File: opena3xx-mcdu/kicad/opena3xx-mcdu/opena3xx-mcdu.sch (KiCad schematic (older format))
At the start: 48 parts, among them J1 Conn_02x01, J2 Conn_02x01, J3 Conn_02x01, J4 Conn_02x01, J5 Raspberry_Pi_Zero, SW1 SW_MEC_5E, U1 MCP23017_SO, U2 MCP23017_SO, U3 MCP23017_SO, U4 MCP23017_SO, U5 MCP23017_SO

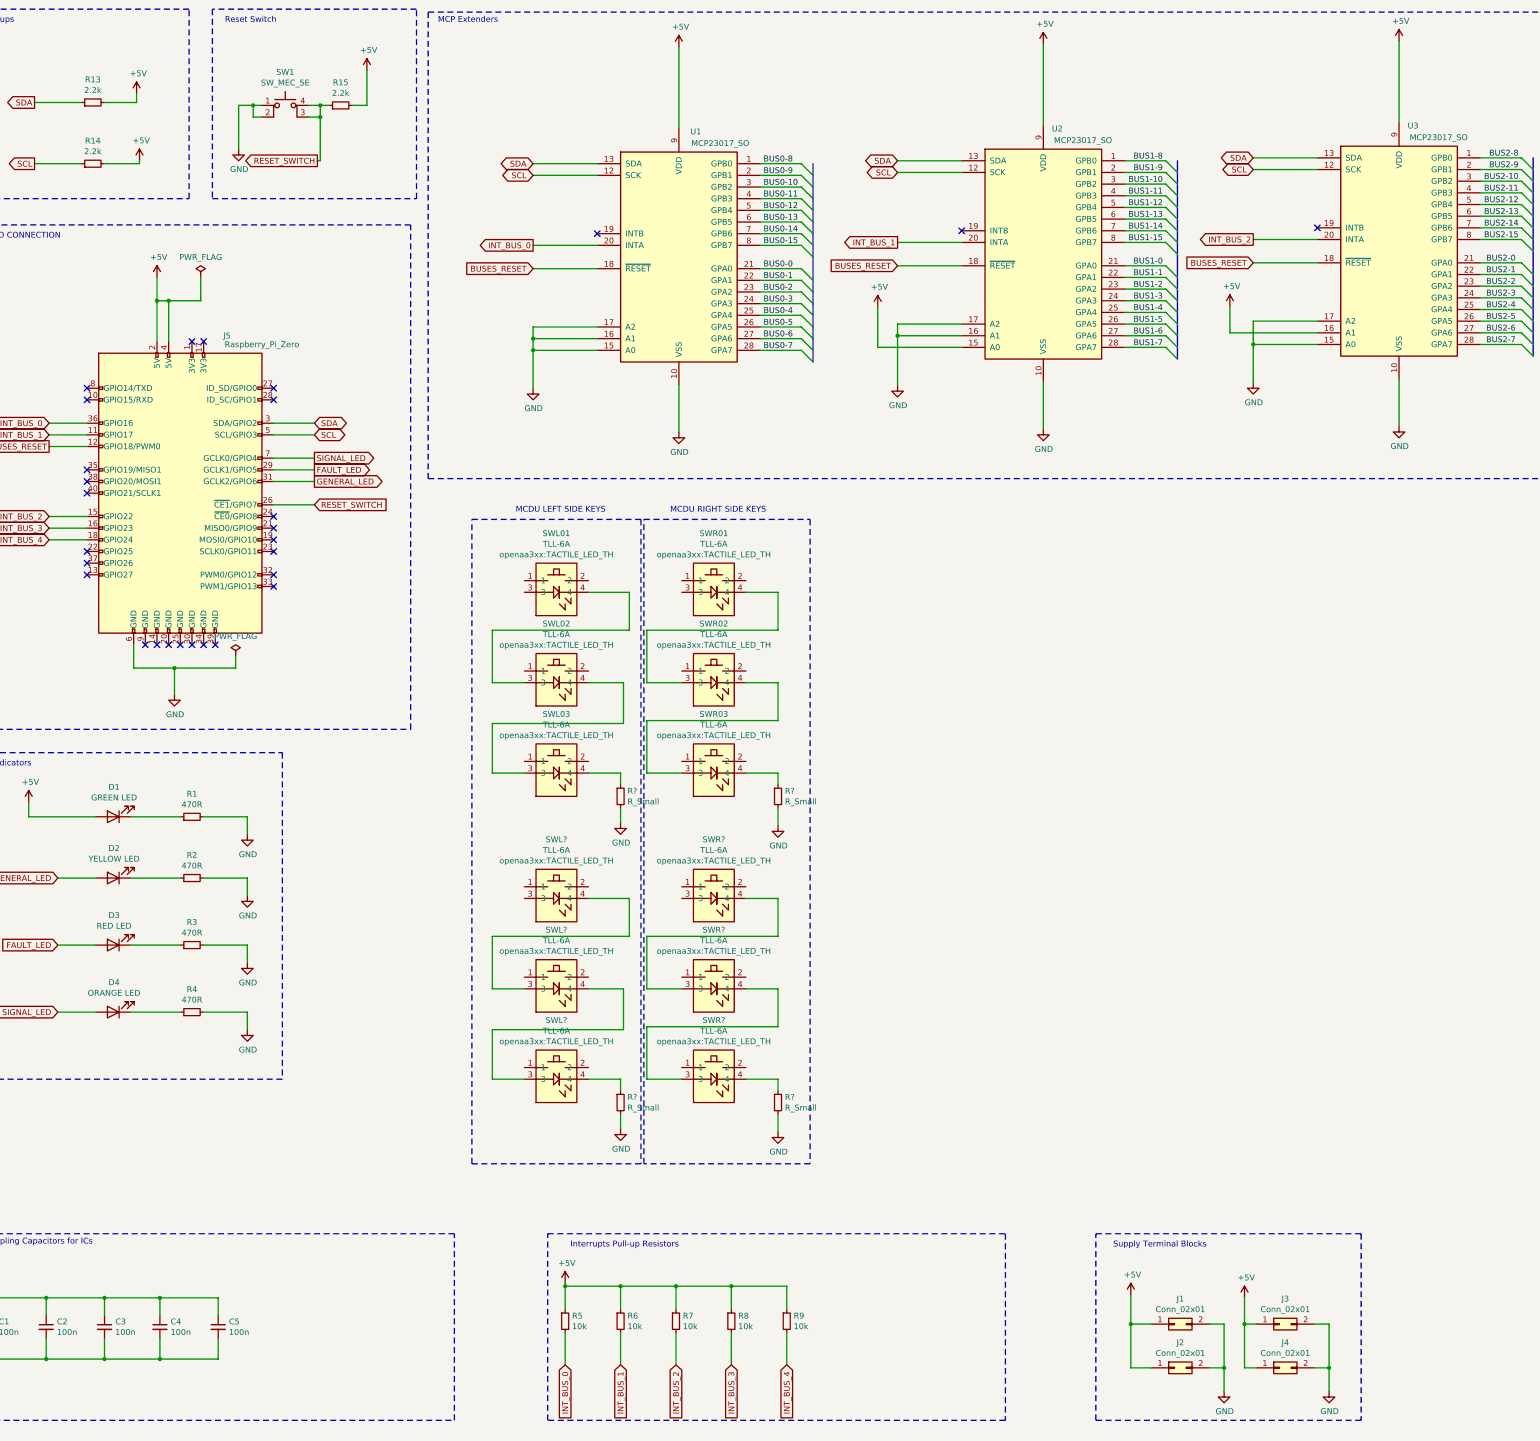
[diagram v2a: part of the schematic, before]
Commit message: Updated MCDU Schematic
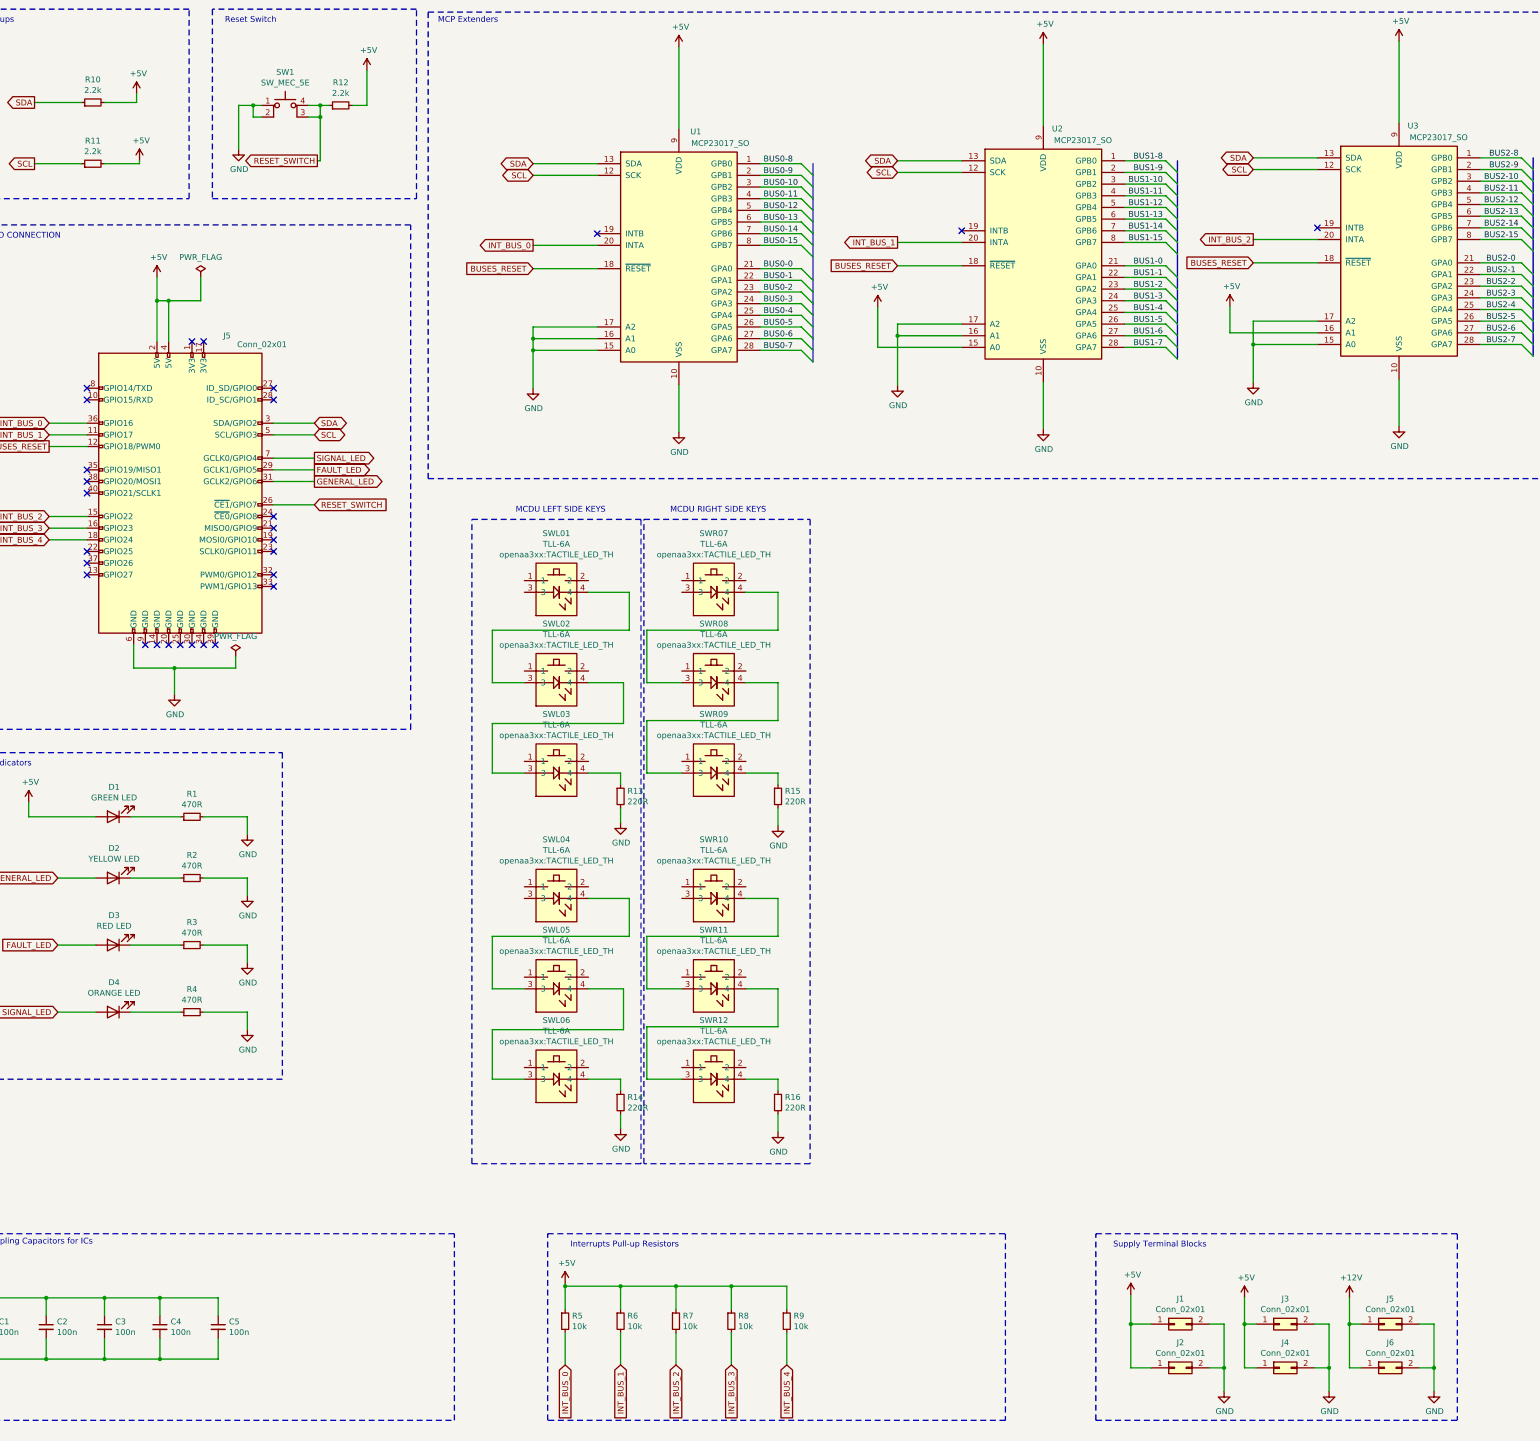
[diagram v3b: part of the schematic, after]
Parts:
- added J5, J6: Conn_02x01, TerminalBlock:TerminalBlock_bornier-2_P5.08mm, symbol Connector_Generic:Conn_02x01
- J5: value Raspberry_Pi_Zero -> Conn_02x01; footprint Connector_PinHeader_2.54mm:PinHeader_2x20_P2.54mm_Vertical -> TerminalBlock:TerminalBlock_bornier-2_P5.08mm
- R13, R14, R15, R16: renamed from R?; value R_Small -> 220R
- gave numbers to parts that had none: 6
- renumbered R13 to R10, R14 to R11, R15 to R12, SWR01 to SWR07, SWR02 to SWR08, SWR03 to SWR09
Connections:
- net GND: now also J5.2 (Pin_2), J6.2 (Pin_2)
- new net +12V: J5.1 (Pin_1), J6.1 (Pin_1)
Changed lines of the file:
@@
 P 2625 4850
 F 0 "J5" H 3025 6200 50  0000 C CNN
-F 1 "Raspberry_Pi_Zero" H 3325 6125 50  0000 C CNN
-F 2 "Connector_PinHeader_2.54mm:PinHeader_2x20_P2.54mm_Vertical" H 2625 4850 50  0001 C CNN
-F 3 "https://www.raspberrypi.org/documentation/hardware/raspberrypi/schematics/rpi_SCH_3bplus_1p0_reduced.pdf" H 2625 4850 50  0001 C CNN
+F 1 "Conn_02x01" H 3325 6125 50  0000 C CNN
+F 2 "TerminalBlock:TerminalBlock_bornier-2_P5.08mm" H 2625 4850 50  0001 C CNN
+F 3 "~" H 2625 4850 50  0001 C CNN
 	1    2625 4850
 	1    0    0    -1
@@
 SCL
 $Comp
-L Device:R_Small R13
+L Device:R_Small R10
 U 1 1 62B8CA36
 P 1875 1500
-F 0 "R13" V 2071 1500 50  0000 C CNN
+F 0 "R10" V 2071 1500 50  0000 C CNN
 F 1 "2.2k" V 1980 1500 50  0000 C CNN
 F 2 "Resistor_SMD:R_1206_3216Metric_Pad1.30x1.75mm_HandSolder" H 1875 1500 50  0001 C CNN
@@
 $EndComp
 $Comp
-L Device:R_Small R14
+L Device:R_Small R11
 U 1 1 62B8D8F0
 P 1875 2025
-F 0 "R14" V 2071 2025 50  0000 C CNN
+F 0 "R11" V 2071 2025 50  0000 C CNN
 F 1 "2.2k" V 1980 2025 50  0000 C CNN
 F 2 "Resistor_SMD:R_1206_3216Metric_Pad1.30x1.75mm_HandSolder" H 1875 2025 50  0001 C CNN
@@
 $EndComp
 Wire Notes Line
-	10475 11200 12750 11200
-Wire Notes Line
-	12750 11200 12750 12800
-Wire Notes Line
-	12750 12800 10475 12800
-Wire Notes Line
 	10475 12800 10475 11200
 Text Notes 11425 11325 2    50   ~ 0
@@
 $EndComp
 $Comp
-L Device:R_Small R15
+L Device:R_Small R12
 U 1 1 60AC11A3
 P 4000 1525
-F 0 "R15" V 4196 1525 50  0000 C CNN
+F 0 "R12" V 4196 1525 50  0000 C CNN
 F 1 "2.2k" V 4105 1525 50  0000 C CNN
 F 2 "Resistor_SMD:R_1206_3216Metric_Pad1.30x1.75mm_HandSolder" H 4000 1525 50  0001 C CNN
@@
 	20625 725  20625 4725
 $Comp
-L opena3xx-kicad:TLL-6A SWR01
+L opena3xx-kicad:TLL-6A SWR07
 U 1 1 60DBB6C4
 P 7125 5400
-F 0 "SWR01" H 7200 5605 50  0000 C CNN
+F 0 "SWR07" H 7200 5605 50  0000 C CNN
 F 1 "TLL-6A" H 7200 5514 50  0000 C CNN
 F 2 "openaa3xx:TACTILE_LED_TH" H 7200 5423 50  0000 C CNN
@@
 $EndComp
 $Comp
-L opena3xx-kicad:TLL-6A SWR02
+L opena3xx-kicad:TLL-6A SWR08
 U 1 1 60DBB6CC
 P 7125 6175
-F 0 "SWR02" H 7200 6380 50  0000 C CNN
+F 0 "SWR08" H 7200 6380 50  0000 C CNN
 F 1 "TLL-6A" H 7200 6289 50  0000 C CNN
 F 2 "openaa3xx:TACTILE_LED_TH" H 7200 6198 50  0000 C CNN
@@
 $EndComp
 $Comp
-L opena3xx-kicad:TLL-6A SWR03
+L opena3xx-kicad:TLL-6A SWR09
 U 1 1 60DBB6D2
 P 7125 6950
-F 0 "SWR03" H 7200 7155 50  0000 C CNN
+F 0 "SWR09" H 7200 7155 50  0000 C CNN
 F 1 "TLL-6A" H 7200 7064 50  0000 C CNN
 F 2 "openaa3xx:TACTILE_LED_TH" H 7200 6973 50  0000 C CNN
@@
 $EndComp
 $Comp
-L Device:R_Small R?
+L Device:R_Small R15
 U 1 1 60DD4B17
 P 7750 7450
-F 0 "R?" H 7809 7496 50  0000 L CNN
-F 1 "R_Small" H 7809 7405 50  0000 L CNN
+F 0 "R15" H 7809 7496 50  0000 L CNN
+F 1 "220R" H 7809 7405 50  0000 L CNN
 F 2 "" H 7750 7450 50  0001 C CNN
 F 3 "~" H 7750 7450 50  0001 C CNN
@@
 	7750 7250 7750 7350
 $Comp
-L power:GND #PWR?
+L power:GND #PWR0122
 U 1 1 60E925BE
 P 7750 7700
-F 0 "#PWR?" H 7750 7450 50  0001 C CNN
+F 0 "#PWR0122" H 7750 7450 50  0001 C CNN
 F 1 "GND" H 7755 7527 50  0000 C CNN
 F 2 "" H 7750 7700 50  0001 C CNN
@@
 	7750 7700 7750 7550
 $Comp
-L opena3xx-kicad:TLL-6A SWR?
+L opena3xx-kicad:TLL-6A SWR10
 U 1 1 60ED204D
 P 7125 8025
-F 0 "SWR?" H 7200 8230 50  0000 C CNN
+F 0 "SWR10" H 7200 8230 50  0000 C CNN
 F 1 "TLL-6A" H 7200 8139 50  0000 C CNN
 F 2 "openaa3xx:TACTILE_LED_TH" H 7200 8048 50  0000 C CNN
@@
 $EndComp
 $Comp
-L opena3xx-kicad:TLL-6A SWR?
+L opena3xx-kicad:TLL-6A SWR11
 U 1 1 60ED2053
 P 7125 8800
-F 0 "SWR?" H 7200 9005 50  0000 C CNN
+F 0 "SWR11" H 7200 9005 50  0000 C CNN
 F 1 "TLL-6A" H 7200 8914 50  0000 C CNN
 F 2 "openaa3xx:TACTILE_LED_TH" H 7200 8823 50  0000 C CNN
@@
 $EndComp
 $Comp
-L opena3xx-kicad:TLL-6A SWR?
+L opena3xx-kicad:TLL-6A SWR12
 U 1 1 60ED2059
 P 7125 9575
-F 0 "SWR?" H 7200 9780 50  0000 C CNN
+F 0 "SWR12" H 7200 9780 50  0000 C CNN
 F 1 "TLL-6A" H 7200 9689 50  0000 C CNN
 F 2 "openaa3xx:TACTILE_LED_TH" H 7200 9598 50  0000 C CNN
@@
 $EndComp
 $Comp
-L Device:R_Small R?
+L Device:R_Small R16
 U 1 1 60ED2065
 P 7750 10075
-F 0 "R?" H 7809 10121 50  0000 L CNN
-F 1 "R_Small" H 7809 10030 50  0000 L CNN
+F 0 "R16" H 7809 10121 50  0000 L CNN
+F 1 "220R" H 7809 10030 50  0000 L CNN
 F 2 "" H 7750 10075 50  0001 C CNN
 F 3 "~" H 7750 10075 50  0001 C CNN
@@
 	7750 9875 7750 9975
 $Comp
-L power:GND #PWR?
+L power:GND #PWR0123
 U 1 1 60ED208A
 P 7750 10325
-F 0 "#PWR?" H 7750 10075 50  0001 C CNN
+F 0 "#PWR0123" H 7750 10075 50  0001 C CNN
 F 1 "GND" H 7755 10152 50  0000 C CNN
 F 2 "" H 7750 10325 50  0001 C CNN
@@
 	6400 10300 6400 10175
 $Comp
-L power:GND #PWR?
+L power:GND #PWR0124
 U 1 1 60ED2077
 P 6400 10300
-F 0 "#PWR?" H 6400 10050 50  0001 C CNN
+F 0 "#PWR0124" H 6400 10050 50  0001 C CNN
 F 1 "GND" H 6405 10127 50  0000 C CNN
 F 2 "" H 6400 10300 50  0001 C CNN
@@
 	6125 9875 6400 9875
 $Comp
-L Device:R_Small R?
+L Device:R_Small R14
 U 1 1 60ED205F
 P 6400 10075
-F 0 "R?" H 6459 10121 50  0000 L CNN
-F 1 "R_Small" H 6459 10030 50  0000 L CNN
+F 0 "R14" H 6459 10121 50  0000 L CNN
+F 1 "220R" H 6459 10030 50  0000 L CNN
 F 2 "" H 6400 10075 50  0001 C CNN
 F 3 "~" H 6400 10075 50  0001 C CNN
@@
 $EndComp
 $Comp
-L opena3xx-kicad:TLL-6A SWL?
+L opena3xx-kicad:TLL-6A SWL06
 U 1 1 60ED2047
 P 5775 9575
-F 0 "SWL?" H 5850 9780 50  0000 C CNN
+F 0 "SWL06" H 5850 9780 50  0000 C CNN
 F 1 "TLL-6A" H 5850 9689 50  0000 C CNN
 F 2 "openaa3xx:TACTILE_LED_TH" H 5850 9598 50  0000 C CNN
@@
 $EndComp
 $Comp
-L opena3xx-kicad:TLL-6A SWL?
+L opena3xx-kicad:TLL-6A SWL05
 U 1 1 60ED2041
 P 5775 8800
-F 0 "SWL?" H 5850 9005 50  0000 C CNN
+F 0 "SWL05" H 5850 9005 50  0000 C CNN
 F 1 "TLL-6A" H 5850 8914 50  0000 C CNN
 F 2 "openaa3xx:TACTILE_LED_TH" H 5850 8823 50  0000 C CNN
@@
 $EndComp
 $Comp
-L opena3xx-kicad:TLL-6A SWL?
+L opena3xx-kicad:TLL-6A SWL04
 U 1 1 60ED203B
 P 5775 8025
-F 0 "SWL?" H 5850 8230 50  0000 C CNN
+F 0 "SWL04" H 5850 8230 50  0000 C CNN
 F 1 "TLL-6A" H 5850 8139 50  0000 C CNN
 F 2 "openaa3xx:TACTILE_LED_TH" H 5850 8048 50  0000 C CNN
@@
 	6400 7675 6400 7550
 $Comp
-L power:GND #PWR?
+L power:GND #PWR0125
 U 1 1 60E18F43
 P 6400 7675
-F 0 "#PWR?" H 6400 7425 50  0001 C CNN
+F 0 "#PWR0125" H 6400 7425 50  0001 C CNN
 F 1 "GND" H 6405 7502 50  0000 C CNN
 F 2 "" H 6400 7675 50  0001 C CNN
@@
 	6125 7250 6400 7250
 $Comp
-L Device:R_Small R?
+L Device:R_Small R13
 U 1 1 60DD1BFB
 P 6400 7450
-F 0 "R?" H 6459 7496 50  0000 L CNN
-F 1 "R_Small" H 6459 7405 50  0000 L CNN
+F 0 "R13" H 6459 7496 50  0000 L CNN
+F 1 "220R" H 6459 7405 50  0000 L CNN
 F 2 "" H 6400 7450 50  0001 C CNN
 F 3 "~" H 6400 7450 50  0001 C CNN
@@
 Wire Notes Line
 	6600 10600 6600 5075
+Text Notes 5500 5025 0    50   ~ 0
+MCDU LEFT SIDE KEYS\n
+Text Notes 6825 5025 0    50   ~ 0
+MCDU RIGHT SIDE KEYS\n
+$Comp
+L Connector_Generic:Conn_02x01 J5
+U 1 1 60F73FB9
+P 12950 11975
+F 0 "J5" H 13000 12192 50  0000 C CNN
+F 1 "Conn_02x01" H 13000 12101 50  0000 C CNN
+F 2 "TerminalBlock:TerminalBlock_bornier-2_P5.08mm" H 12950 11975 50  0001 C CNN
+F 3 "~" H 12950 11975 50  0001 C CNN
+	1    12950 11975
+	1    0    0    -1
+$EndComp
+Wire Wire Line
+	12650 11975 12750 11975
+Wire Wire Line
+	12750 12350 12650 12350
+Wire Wire Line
+	12650 12350 12650 11975
+Connection ~ 12650 11975
+$Comp
+L power:GND #PWR0126
+U 1 1 60F73FCA
+P 13375 12550
+F 0 "#PWR0126" H 13375 12300 50  0001 C CNN
+F 1 "GND" H 13380 12377 50  0000 C CNN
+F 2 "" H 13375 12550 50  0001 C CNN
+F 3 "" H 13375 12550 50  0001 C CNN
+	1    13375 12550
+	1    0    0    -1
+$EndComp
+Wire Wire Line
+	13375 12550 13375 12350
+Wire Wire Line
+	13375 12350 13250 12350
+Wire Wire Line
+	13375 12350 13375 11975
+Wire Wire Line
+	13375 11975 13250 11975
+Connection ~ 13375 12350
+$Comp
+L Connector_Generic:Conn_02x01 J6
+U 1 1 60F73FD5
+P 12950 12350
+F 0 "J6" H 13000 12567 50  0000 C CNN
+F 1 "Conn_02x01" H 13000 12476 50  0000 C CNN
+F 2 "TerminalBlock:TerminalBlock_bornier-2_P5.08mm" H 12950 12350 50  0001 C CNN
+F 3 "~" H 12950 12350 50  0001 C CNN
+	1    12950 12350
+	1    0    0    -1
+$EndComp
+$Comp
+L power:+12V #PWR0127
+U 1 1 60F93B82
+P 12650 11750
+F 0 "#PWR0127" H 12650 11600 50  0001 C CNN
+F 1 "+12V" H 12665 11923 50  0000 C CNN
+F 2 "" H 12650 11750 50  0001 C CNN
+F 3 "" H 12650 11750 50  0001 C CNN
+	1    12650 11750
+	1    0    0    -1
+$EndComp
+Wire Notes Line
+	10475 11200 13575 11200
+Wire Notes Line
+	13575 11200 13575 12800
+Wire Notes Line
+	10475 12800 13575 12800
 Wire Bus Line
 	20375 1975 20375 3675
@@
 Wire Bus Line
 	8050 2025 8050 3725
-Text Notes 5500 5025 0    50   ~ 0
-MCDU LEFT SIDE KEYS\n
-Text Notes 6825 5025 0    50   ~ 0
-MCDU RIGHT SIDE KEYS\n
+Wire Wire Line
+	12650 11750 12650 11975
 $EndSCHEMATC

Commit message: MCDU Updates
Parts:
- added J8, J9: Conn_02x01, TerminalBlock:TerminalBlock_bornier-2_P5.08mm, symbol Connector_Generic:Conn_02x01
- J5: footprint TerminalBlock:TerminalBlock_bornier-2_P5.08mm -> Connector_PinHeader_2.54mm:PinHeader_2x20_P2.54mm_Vertical
- R13, R14, R15, R16: footprint (none) -> Resistor_SMD:R_1210_3225Metric_Pad1.30x2.65mm_HandSolder
- renumbered J5 to J6, J6 to J7, SWR07 to SWR01, SWR08 to SWR02, SWR09 to SWR03, SWR10 to SWR04, SWR11 to SWR05, SWR12 to SWR06
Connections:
- net +12V: now also SWL01.3, SWL04.3, SWR01.3, SWR04.3, J8.1 (Pin_1), J9.1 (Pin_1)
- net BUS0-0: now also SWL01.1
- net BUS0-1: now also SWL02.1
- net BUS0-10: now also SWR05.1
- net BUS0-11: now also SWR06.1
- net BUS0-2: now also SWL03.1
- net BUS0-3: now also SWL04.1
- net BUS0-4: now also SWL05.1
- net BUS0-5: now also SWL06.1
- net BUS0-6: now also SWR01.1
- net BUS0-7: now also SWR02.1
- net BUS0-8: now also SWR03.1
- net BUS0-9: now also SWR04.1
- net GND: now also SWL01.2, SWL03.2, SWL04.2, SWL05.2, SWL06.2, SWR01.2, SWR02.2, SWR03.2, SWR04.2, SWR05.2, SWR06.2, J8.2 (Pin_2), J9.2 (Pin_2)
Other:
- note added: "Supply Terminal Blocks\n5V & 12V Variable for Backlight\n"
- note removed: "Supply Terminal Blocks\n"

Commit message: Updates MCDU Schematic
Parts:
- added R17, R18, R19, R20, R21, R22, R23, R24: 220R, Resistor_SMD:R_1210_3225Metric_Pad1.30x2.65mm_HandSolder, symbol Device:R_Small
- added SW13, SW14, SW15, SW16, SW17, SW18, SW19, SW20, SW21, SW22, SW23, SW24, SW25, SW26, SW27, SW28, SW29, SW30, SW31, SW32, SW33, SW34, SW35, SW36: TLL-6A, openaa3xx:TACTILE_LED_TH, symbol opena3xx-kicad:TLL-6A
- SW1: renamed from SWL01; MCDU IO Name (none) -> LSK1
- SW10: renamed from SWR04; MCDU IO Name (none) -> RSK4
- SW11: renamed from SWR05; MCDU IO Name (none) -> RSK5
- SW12: renamed from SWR06; MCDU IO Name (none) -> RSK6
- SW2: renamed from SWL02; MCDU IO Name (none) -> LSK2
- SW3: renamed from SWL03; MCDU IO Name (none) -> LSK3
- SW4: renamed from SWL04; MCDU IO Name (none) -> LSK4
- SW5: renamed from SWL05; MCDU IO Name (none) -> LSK5
- SW6: renamed from SWL06; MCDU IO Name (none) -> LSK6
- SW7: renamed from SWR01; MCDU IO Name (none) -> RSK1
- SW8: renamed from SWR02; MCDU IO Name (none) -> RSK2
- SW9: renamed from SWR03; MCDU IO Name (none) -> RSK3
- renumbered SW1 to SW100
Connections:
- net +12V: now also SW13.3, SW16.3, SW19.3, SW22.3, SW25.3, SW28.3, SW31.3, SW34.3
- net BUS0-12: now also SW13.1
- net BUS0-13: now also SW14.1
- net BUS0-14: now also SW15.1
- net BUS0-15: now also SW16.1
- net BUS1-0: now also SW17.1
- net BUS1-1: now also SW18.1
- net BUS1-10: now also SW27.1
- net BUS1-11: now also SW28.1
- net BUS1-12: now also SW29.1
- net BUS1-13: now also SW30.1
- net BUS1-14: now also SW31.1
- net BUS1-15: now also SW32.1
- net BUS1-2: now also SW19.1
- net BUS1-3: now also SW20.1
- net BUS1-4: now also SW21.1
- net BUS1-5: now also SW22.1
- net BUS1-6: now also SW23.1
- net BUS1-7: now also SW24.1
- net BUS1-8: now also SW25.1
- net BUS1-9: now also SW26.1
- net BUS2-0: now also SW33.1
- net BUS2-1: now also SW34.1
- net BUS2-2: now also SW35.1
- net BUS2-3: now also SW36.1
- net GND: now also SW2.2, R17.2, R18.2, R19.2, R20.2, R21.2, R22.2, R23.2, R24.2, SW13.2, SW14.2, SW15.2, SW16.2, SW17.2, SW18.2, SW19.2, SW20.2, SW21.2, SW22.2, SW23.2, SW24.2, SW25.2, SW26.2, SW27.2, SW28.2, SW29.2, SW30.2, SW31.2, SW32.2, SW33.2, SW34.2, SW35.2, SW36.2
- new net: SW19.4, SW20.3
- new net: SW20.4, SW21.3
- new net: R19.1, SW21.4
- new net: SW22.4, SW23.3
- new net: SW23.4, SW24.3
- new net: R20.1, SW24.4
- new net: R18.1, SW18.4
- new net: SW17.4, SW18.3
- new net: SW16.4, SW17.3
- new net: R17.1, SW15.4
- new net: SW14.4, SW15.3
- new net: SW13.4, SW14.3
- new net: SW31.4, SW32.3
- new net: SW32.4, SW33.3
- new net: R23.1, SW33.4
- new net: SW34.4, SW35.3
- new net: SW35.4, SW36.3
- new net: R24.1, SW36.4
- new net: R22.1, SW30.4
- new net: SW29.4, SW30.3
- new net: SW28.4, SW29.3
- new net: R21.1, SW27.4
- new net: SW26.4, SW27.3
- new net: SW25.4, SW26.3
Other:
- note added: "MCDU MENU KEYS\n\n"
- note added: "MCDU NUMERIC KEYS\n"
- moved on the sheet: C1, C2, C3, C4, C5, J1, J2, J3, J4, J6, J7, J8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
